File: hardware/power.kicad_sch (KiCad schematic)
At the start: 8 parts, among them J7 USB_C_Receptacle_USB2.0_16P, U5 USBLC6-2P6, U6 AP7361C-33E

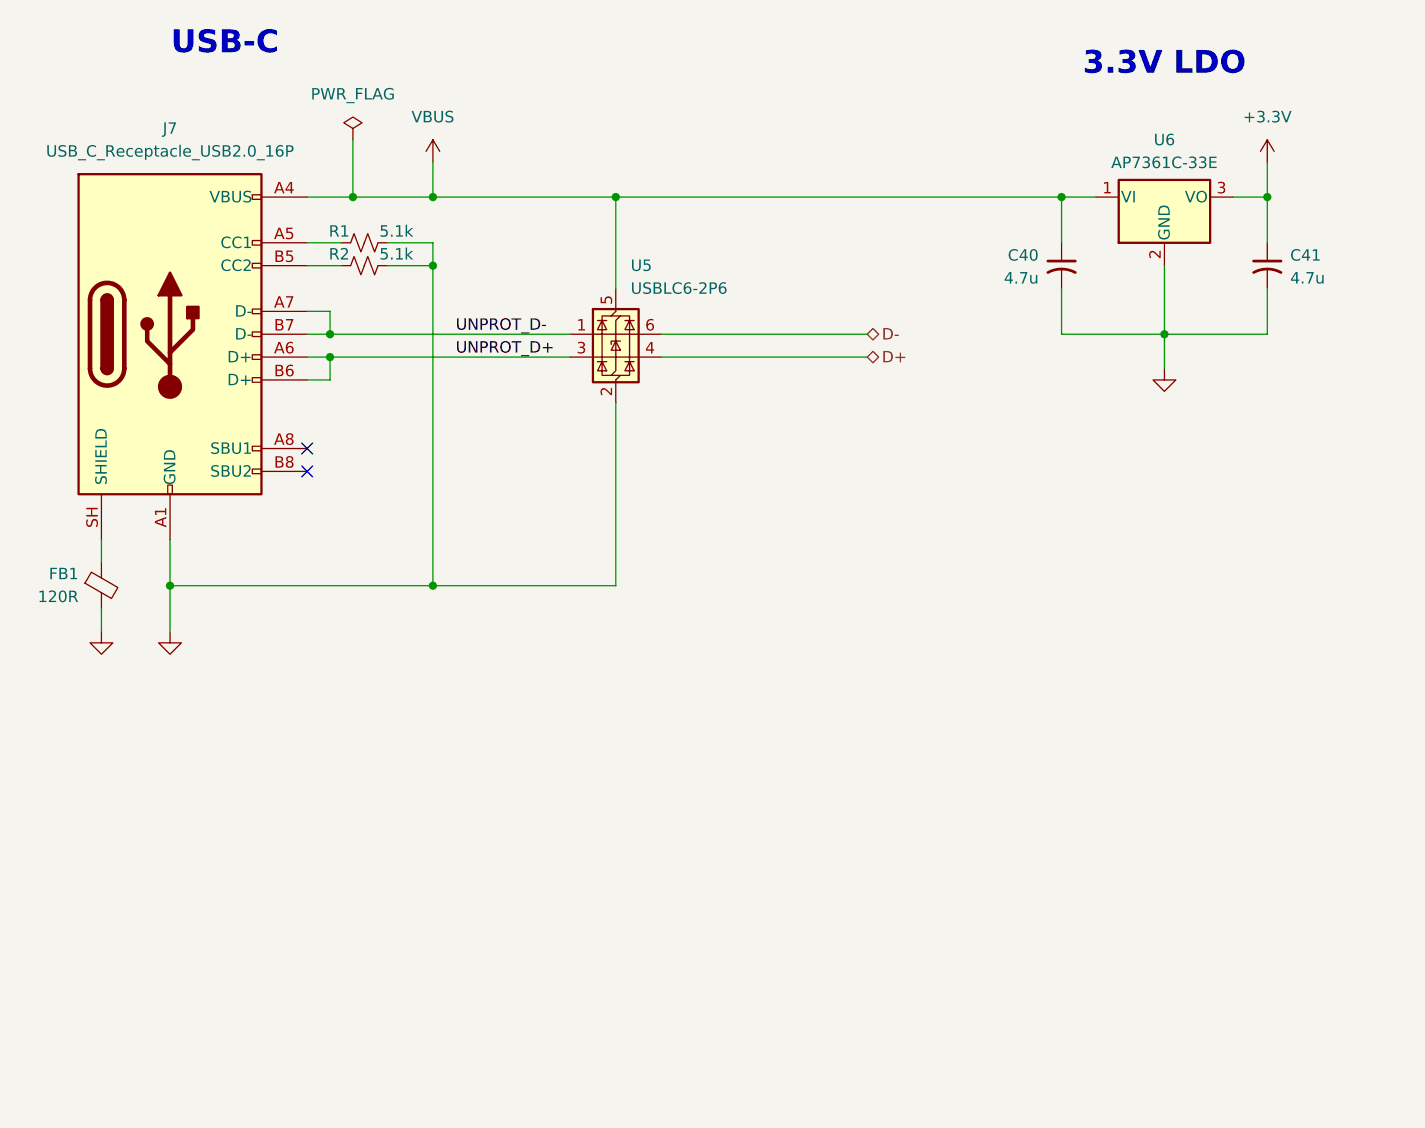
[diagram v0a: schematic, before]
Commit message: start rearranging layout
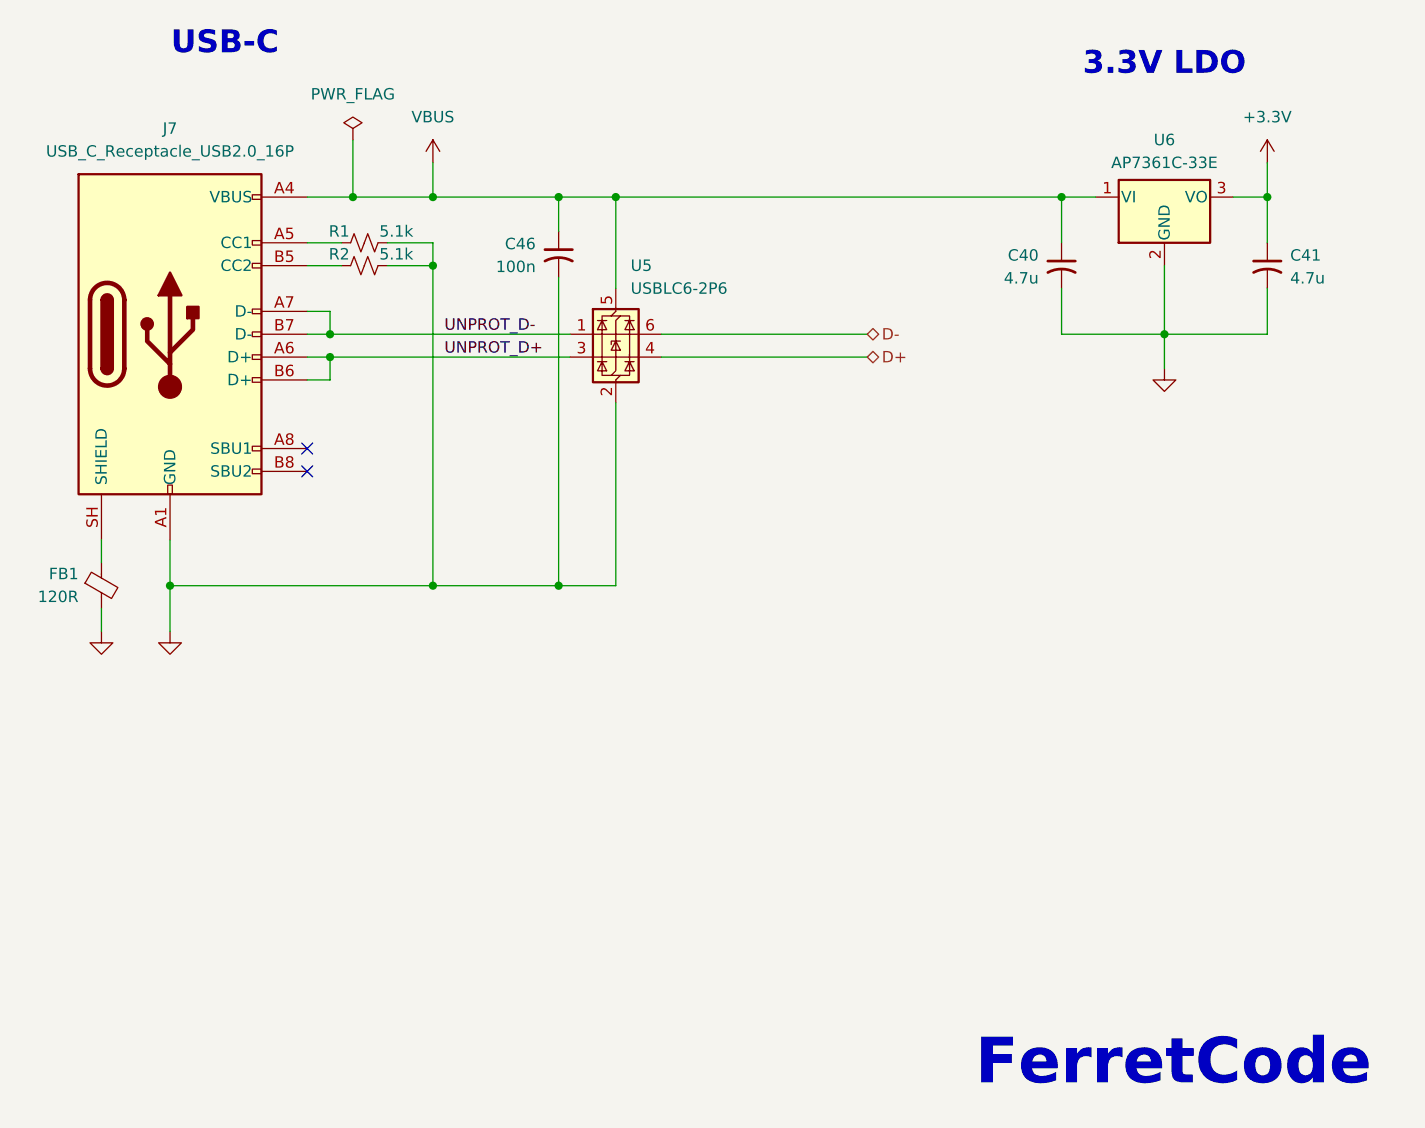
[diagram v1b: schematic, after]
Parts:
- added C46: 100n, Capacitor_SMD:C_0402_1005Metric, symbol Device:C_Small_US
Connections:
- net GND: now also C46.2
- net VBUS: now also C46.1
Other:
- note added: "FerretCode"
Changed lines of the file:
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@@
+		)
+	)
+	(text "FerretCode"
+		(exclude_from_sim no)
+		(at 197.866 177.546 0)
+		(effects
+			(font
+				(size 5.08 5.08)
+				(thickness 1.016)
+				(bold yes)
+			)
 		)
 	)
@@
 	)
 	(junction
+		(at 129.54 81.28)
+		(diameter 0)
+		(color 0 0 0 0)
+	)
+	(junction
 		(at 196.85 96.52)
 		(diameter 0)
@@
 	)
 	(junction
+		(at 129.54 124.46)
+		(diameter 0)
+		(color 0 0 0 0)
+	)
+	(junction
 		(at 208.28 81.28)
 		(diameter 0)
@@
 	(wire
 		(pts
+			(xy 129.54 81.28) (xy 135.89 81.28)
+		)
+		(stroke
+			(width 0)
+			(type default)
+		)
+	)
+	(wire
+		(pts
 			(xy 101.6 86.36) (xy 105.41 86.36)
 		)
@@
 	(wire
 		(pts
-			(xy 115.57 81.28) (xy 135.89 81.28)
+			(xy 115.57 81.28) (xy 129.54 81.28)
 		)
 		(stroke
@@
 	(wire
 		(pts
+			(xy 129.54 81.28) (xy 129.54 85.09)
+		)
+		(stroke
+			(width 0)
+			(type default)
+		)
+	)
+	(wire
+		(pts
 			(xy 104.14 99.06) (xy 130.81 99.06)
 		)
@@
 	(wire
 		(pts
+			(xy 129.54 90.17) (xy 129.54 124.46)
+		)
+		(stroke
+			(width 0)
+			(type default)
+		)
+	)
+	(wire
+		(pts
 			(xy 115.57 86.36) (xy 115.57 88.9)
 		)
@@
 	(wire
 		(pts
+			(xy 129.54 124.46) (xy 115.57 124.46)
+		)
+		(stroke
+			(width 0)
+			(type default)
+		)
+	)
+	(wire
+		(pts
 			(xy 208.28 91.44) (xy 208.28 96.52)
 		)
@@
 	(wire
 		(pts
-			(xy 135.89 124.46) (xy 115.57 124.46)
+			(xy 135.89 124.46) (xy 129.54 124.46)
 		)
 		(stroke
@@
 	)
 	(label "UNPROT_D+"
-		(at 118.11 99.06 0)
+		(at 116.84 99.06 0)
 		(effects
 			(font
@@
 	)
 	(label "UNPROT_D-"
-		(at 118.11 96.52 0)
+		(at 116.84 96.52 0)
 		(effects
 			(font
@@
 					(unit 1)
 				)
+			)
+		)
+	)
+	(symbol
+		(lib_id "Device:C_Small_US")
+		(at 129.54 87.63 0)
+		(mirror y)
+		(unit 1)
+		(body_style 1)
+		(exclude_from_sim no)
+		(in_bom yes)
+		(on_board yes)
+		(in_pos_files yes)
+		(dnp no)
+		(property "Reference" "C46"
+			(at 127 86.4869 0)
+			(show_name no)
+			(do_not_autoplace no)
+			(effects
+				(font
+					(size 1.27 1.27)
+				)
+				(justify left)
+			)
+		)
+		(property "Value" "100n"
+			(at 127 89.0269 0)
+			(show_name no)
+			(do_not_autoplace no)
+			(effects
+				(font
+					(size 1.27 1.27)
+				)
+				(justify left)
+			)
+		)
+		(property "Footprint" "Capacitor_SMD:C_0402_1005Metric"
+			(at 129.54 87.63 0)
+			(hide yes)
+			(show_name no)
+			(do_not_autoplace no)
+			(effects
+				(font
+					(size 1.27 1.27)
+				)
+			)
+		)
+		(property "Datasheet" ""
+			(at 129.54 87.63 0)
+			(hide yes)
+			(show_name no)
+			(do_not_autoplace no)
+			(effects
+				(font
+					(size 1.27 1.27)
+				)
+			)
+		)
+		(property "Description" "capacitor, small US symbol"
+			(at 129.54 87.63 0)
+			(hide yes)
+			(show_name no)
+			(do_not_autoplace no)
+			(effects
+				(font
+					(size 1.27 1.27)
+				)
+			)
+		)
+		(pin "1"
+		)
+		(pin "2"
+		)
+		(instances
+			(project "ns-1"
+				(path "/978de24d-6500-499f-ae29-c28fdde180f3/992bb2e3-ed1b-4e7d-9201-5dcf9e53f1a9"
+					(reference "C46")
+					(unit 1)
+				)

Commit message: finalize respin
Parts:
- C40, C41: LCSC PN (none) -> C1779
- C46: LCSC PN (none) -> C1525
- J7: LCSC PN C3197899 -> C165948
- R1, R2: LCSC PN C2906874 -> C23186
- U5: LCSC PN (none) -> C2827693
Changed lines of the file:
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@@
+			)
+		)
+		(property "LCSC PN" "C2827693"
+			(at 135.89 96.52 0)
+			(hide yes)
+			(show_name no)
+			(do_not_autoplace no)
+			(effects
+				(font
+					(size 1.27 1.27)
+				)
 			)
 		)
@@
 		)
 		(property "Description" "capacitor, small US symbol"
+			(at 185.42 88.9 0)
+			(hide yes)
+			(show_name no)
+			(do_not_autoplace no)
+			(effects
+				(font
+					(size 1.27 1.27)
+				)
+			)
+		)
+		(property "LCSC PN" "C1779"
 			(at 185.42 88.9 0)
 			(hide yes)
@@
 			)
 		)
-		(property "LCSC PN" "C3197899"
+		(property "LCSC PN" "C165948"
 			(at 86.36 96.52 0)
 			(hide yes)
@@
 			)
 		)
+		(property "LCSC PN" "C1525"
+			(at 129.54 87.63 0)
+			(hide yes)
+			(show_name no)
+			(do_not_autoplace no)
+			(effects
+				(font
+					(size 1.27 1.27)
+				)
+			)
+		)
 		(pin "1"
 		)
@@
 			)
 		)
+		(property "LCSC PN" "C1779"
+			(at 208.28 88.9 0)
+			(hide yes)
+			(show_name no)
+			(do_not_autoplace no)
+			(effects
+				(font
+					(size 1.27 1.27)
+				)
+			)
+		)
 		(pin "2"
 		)
@@
 			)
 		)
-		(property "LCSC PN" "C2906874"
+		(property "LCSC PN" " C23186"
 			(at 107.95 86.36 90)
 			(hide yes)
@@
 			)
 		)
-		(property "LCSC PN" "C2906874"
+		(property "LCSC PN" " C23186"
 			(at 107.95 88.9 90)
 			(hide yes)
